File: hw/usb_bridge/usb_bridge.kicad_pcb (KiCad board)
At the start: 2 copper layers, 51 x 31 mm, 74 parts, among them J1 USB_C_Receptacle_USB2.0_14P, J2 DE9, J3 SWD, J4 BOOT, U1 CH340E, U2 MAX485E, U3 CH334R, U5 MCP1754S-3302xCB, U6 TJA1051T-3, U7 STM32G0B1CBT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

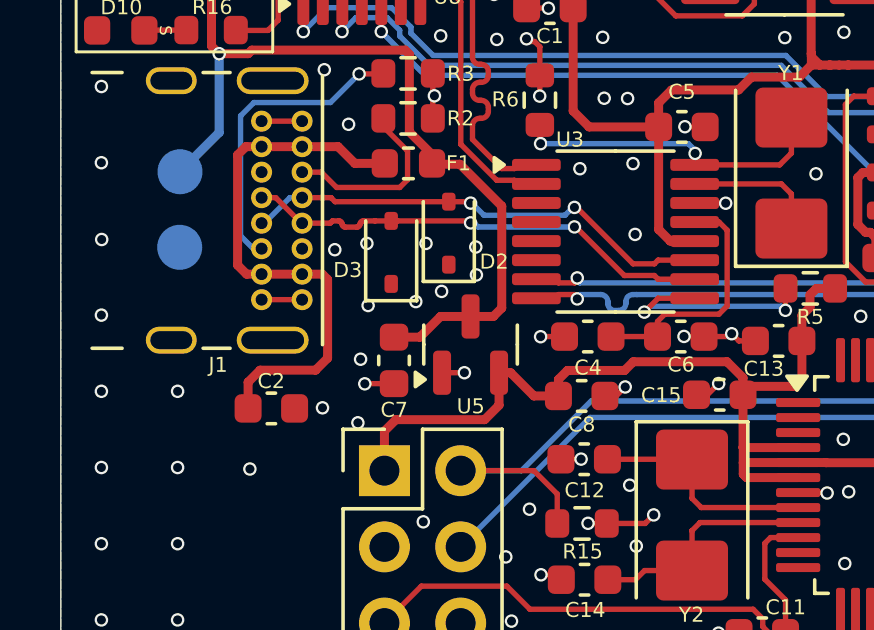
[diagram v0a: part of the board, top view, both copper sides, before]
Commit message: Replace USB-C TVS with working ones, replace footprint of TVS to hand solder version
Signed-off-by: Mateusz Pajak <22417805+Tai-Min@users.noreply.github.com>
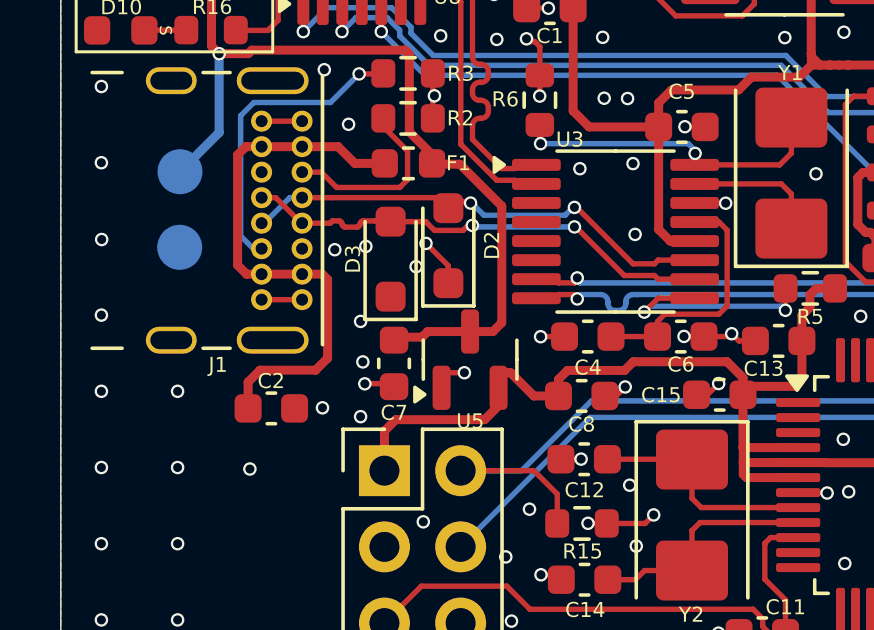
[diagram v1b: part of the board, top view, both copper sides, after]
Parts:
- D2, D3: value PTVSHC3D4V5B -> PESD5V0S1BA; footprint Diode_SMD:D_SOD-323 -> Diode_SMD:D_SOD-323_HandSoldering
- moved U5 0.50 mm to (140.1, 107.0)
- moved D2 0.42 mm to (139.4, 103.2)
- moved D3 0.23 mm to (137.4, 103.7)
- moved C7 0.10 mm to (137.6, 107.2)
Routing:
- net GND: track 32.4 -> 34.0 mm, vias 167 -> 164
